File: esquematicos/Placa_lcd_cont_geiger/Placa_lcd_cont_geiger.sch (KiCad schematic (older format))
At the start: 17 parts, among them J1 Conn_02x04_Counter_Clockwise, J2 Conn_01x14_Female, J3 Conn_01x04_Female, P1 Power, P2 Analog, P3 Digital, P4 Digital, Q1 BC548, Q2 BC548

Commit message: Agregado del PCB del teclado(2)
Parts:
- J3: footprint Connector_JST:JST_EH_B04B-EH-A_1x04_P2.50mm_Vertical -> Connector_JST:JST_XH_B04B-XH-A_1x04_P2.50mm_Vertical
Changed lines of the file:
@@
 F 0 "J3" V 3940 3612 50  0000 R CNN
 F 1 "Conn_01x04_Female" V 3849 3612 50  0000 R CNN
-F 2 "Connector_JST:JST_EH_B04B-EH-A_1x04_P2.50mm_Vertical" H 4000 3900 50  0001 C CNN
+F 2 "Connector_JST:JST_XH_B04B-XH-A_1x04_P2.50mm_Vertical" H 4000 3900 50  0001 C CNN
 F 3 "~" H 4000 3900 50  0001 C CNN
 	1    4000 3900

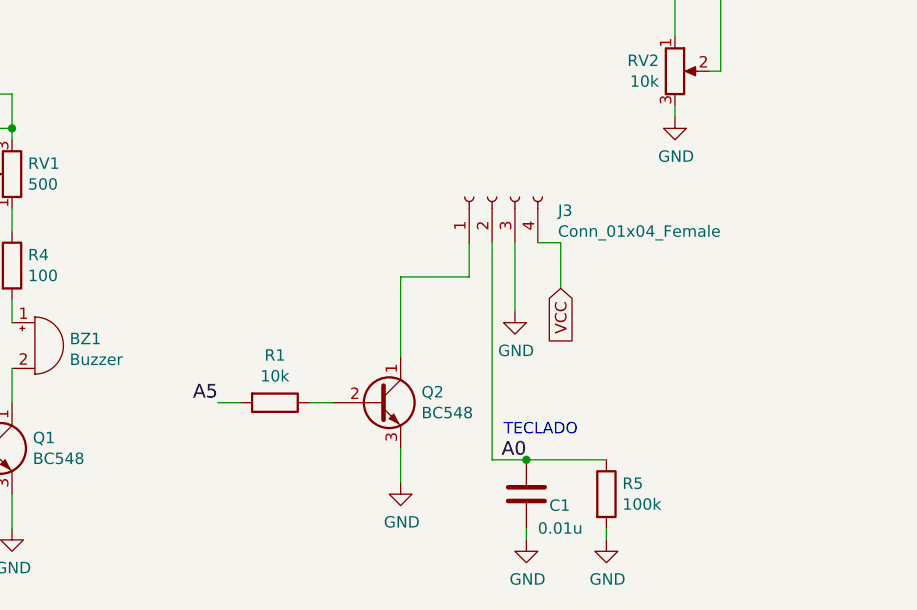
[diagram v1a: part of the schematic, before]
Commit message: Agregado de LED verde a la placa del teclado e incremento de las dimensiones de esta última incluyendo una mayor separación entre los botones
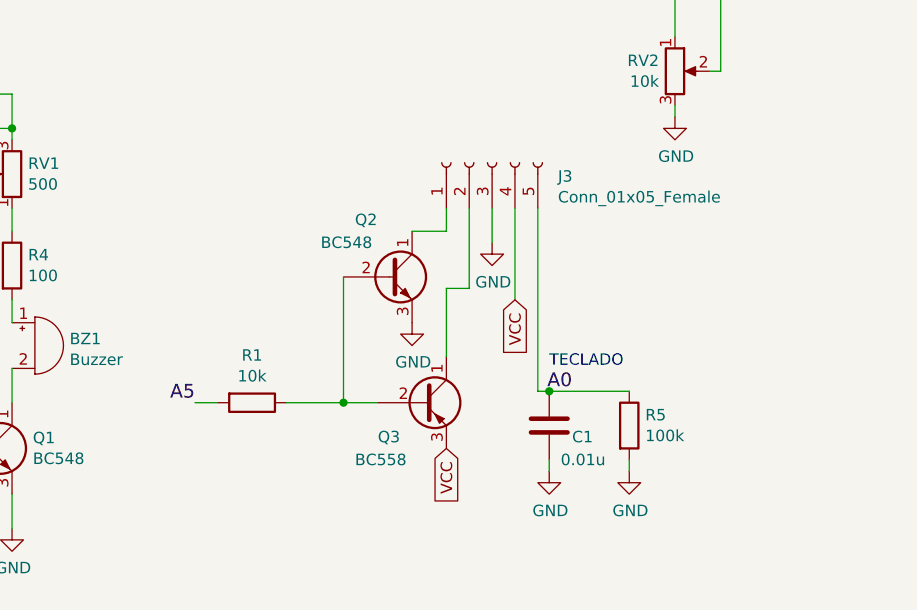
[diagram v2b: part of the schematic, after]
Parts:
- removed J3: Conn_01x04_Female, Connector_JST:JST_XH_B04B-XH-A_1x04_P2.50mm_Vertical, symbol Connector:Conn_01x04_Female
- added J3: Conn_01x05_Female, Connector_JST:JST_XH_B05B-XH-A_1x05_P2.50mm_Vertical, symbol Connector:Conn_01x05_Female
- added Q3: BC558, Package_TO_SOT_THT:TO-92_Inline, symbol Transistor_BJT:BC558
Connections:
- net +5V: now also J3.4 (Pin_4), Q3.3 (E)
- net A0: now also J3.5 (Pin_5)
- net GND: now also J3.3 (Pin_3)
- net at Q2.2 (B), R1.1: now also Q3.2 (B)
- net at Q2.1 (C): now also J3.1 (Pin_1)
- new net: J3.2 (Pin_2), Q3.1 (C)
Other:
- moved on the sheet: C1, Q2, R1, R5
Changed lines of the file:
@@
 	8250 1850 8100 1850
-$Comp
-L power:GND #PWR05
-U 1 1 5D57300A
-P 3600 5150
-F 0 "#PWR05" H 3600 4900 50  0001 C CNN
-F 1 "GND" H 3605 4977 50  0000 C CNN
-F 2 "" H 3600 5150 50  0001 C CNN
-F 3 "" H 3600 5150 50  0001 C CNN
-	1    3600 5150
-	1    0    0    -1
-$EndComp
-Wire Wire Line
-	3600 5150 3600 5000
 $Comp
 L Device:R R1
 U 1 1 5D574156
-P 3050 4800
-F 0 "R1" V 2843 4800 50  0000 C CNN
-F 1 "10k" V 2934 4800 50  0000 C CNN
-F 2 "Resistor_THT:R_Axial_DIN0207_L6.3mm_D2.5mm_P10.16mm_Horizontal" V 2980 4800 50  0001 C CNN
-F 3 "~" H 3050 4800 50  0001 C CNN
-	1    3050 4800
+P 2950 4800
+F 0 "R1" V 2743 4800 50  0000 C CNN
+F 1 "10k" V 2834 4800 50  0000 C CNN
+F 2 "Resistor_THT:R_Axial_DIN0207_L6.3mm_D2.5mm_P10.16mm_Horizontal" V 2880 4800 50  0001 C CNN
+F 3 "~" H 2950 4800 50  0001 C CNN
+	1    2950 4800
 	0    1    1    0
 $EndComp
-Wire Wire Line
-	3300 4800 3200 4800
-Wire Wire Line
-	2900 4800 2800 4800
 Text GLabel 1800 3450 0    50   Input ~ 0
 VCC
@@
 Wire Wire Line
 	2300 2000 2300 2050
-Text GLabel 4300 4300 3    50   Input ~ 0
+Text GLabel 4100 4350 3    50   Input ~ 0
 VCC
-Wire Wire Line
-	4300 4300 4300 4100
-Wire Wire Line
-	4300 4100 4200 4100
 $Comp
 L power:GND #PWR013
 U 1 1 5D5B0045
-P 4100 4400
-F 0 "#PWR013" H 4100 4150 50  0001 C CNN
-F 1 "GND" H 4105 4227 50  0000 C CNN
-F 2 "" H 4100 4400 50  0001 C CNN
-F 3 "" H 4100 4400 50  0001 C CNN
-	1    4100 4400
-	1    0    0    -1
-$EndComp
-Wire Wire Line
-	4100 4400 4100 4100
+P 4000 4100
+F 0 "#PWR013" H 4000 3850 50  0001 C CNN
+F 1 "GND" H 4005 3927 50  0000 C CNN
+F 2 "" H 4000 4100 50  0001 C CNN
+F 3 "" H 4000 4100 50  0001 C CNN
+	1    4000 4100
+	1    0    0    -1
+$EndComp
 $Comp
 L Device:R R5
 U 1 1 5D5B29A8
-P 4500 5200
-F 0 "R5" H 4570 5246 50  0000 L CNN
-F 1 "100k" H 4570 5155 50  0000 L CNN
-F 2 "Resistor_THT:R_Axial_DIN0207_L6.3mm_D2.5mm_P10.16mm_Horizontal" V 4430 5200 50  0001 C CNN
-F 3 "~" H 4500 5200 50  0001 C CNN
-	1    4500 5200
+P 4600 4900
+F 0 "R5" H 4670 4946 50  0000 L CNN
+F 1 "100k" H 4670 4855 50  0000 L CNN
+F 2 "Resistor_THT:R_Axial_DIN0207_L6.3mm_D2.5mm_P10.16mm_Horizontal" V 4530 4900 50  0001 C CNN
+F 3 "~" H 4600 4900 50  0001 C CNN
+	1    4600 4900
 	1    0    0    -1
 $EndComp
@@
 L Device:C C1
 U 1 1 5D5B30AC
-P 4150 5200
-F 0 "C1" H 4250 5150 50  0000 L CNN
-F 1 "0.01u" H 4200 5050 50  0000 L CNN
-F 2 "Capacitor_THT:C_Axial_L5.1mm_D3.1mm_P7.50mm_Horizontal" H 4188 5050 50  0001 C CNN
-F 3 "~" H 4150 5200 50  0001 C CNN
-	1    4150 5200
+P 4250 4900
+F 0 "C1" H 4350 4850 50  0000 L CNN
+F 1 "0.01u" H 4300 4750 50  0000 L CNN
+F 2 "Capacitor_THT:C_Axial_L5.1mm_D3.1mm_P7.50mm_Horizontal" H 4288 4750 50  0001 C CNN
+F 3 "~" H 4250 4900 50  0001 C CNN
+	1    4250 4900
 	1    0    0    -1
 $EndComp
@@
 L power:GND #PWR012
 U 1 1 5D5BA3C4
-P 4500 5400
-F 0 "#PWR012" H 4500 5150 50  0001 C CNN
-F 1 "GND" H 4505 5227 50  0000 C CNN
-F 2 "" H 4500 5400 50  0001 C CNN
-F 3 "" H 4500 5400 50  0001 C CNN
-	1    4500 5400
-	1    0    0    -1
-$EndComp
-Wire Wire Line
-	4500 5400 4500 5350
+P 4600 5100
+F 0 "#PWR012" H 4600 4850 50  0001 C CNN
+F 1 "GND" H 4605 4927 50  0000 C CNN
+F 2 "" H 4600 5100 50  0001 C CNN
+F 3 "" H 4600 5100 50  0001 C CNN
+	1    4600 5100
+	1    0    0    -1
+$EndComp
+Wire Wire Line
+	4600 5100 4600 5050
 $Comp
 L power:GND #PWR011
 U 1 1 5D5BCCB6
-P 4150 5400
-F 0 "#PWR011" H 4150 5150 50  0001 C CNN
-F 1 "GND" H 4155 5227 50  0000 C CNN
-F 2 "" H 4150 5400 50  0001 C CNN
-F 3 "" H 4150 5400 50  0001 C CNN
-	1    4150 5400
-	1    0    0    -1
-$EndComp
-Wire Wire Line
-	4150 5400 4150 5350
-Text Label 4150 5050 2    60   ~ 0
-A0
-Text Notes 4050 4950 0    50   ~ 0
+P 4250 5100
+F 0 "#PWR011" H 4250 4850 50  0001 C CNN
+F 1 "GND" H 4255 4927 50  0000 C CNN
+F 2 "" H 4250 5100 50  0001 C CNN
+F 3 "" H 4250 5100 50  0001 C CNN
+	1    4250 5100
+	1    0    0    -1
+$EndComp
+Wire Wire Line
+	4250 5100 4250 5050
+Text Notes 4250 4650 0    50   ~ 0
 TECLADO
 Wire Wire Line
-	4150 5050 4500 5050
-$Comp
-L Connector:Conn_01x04_Female J3
-U 1 1 5D58CA04
-P 4000 3900
-F 0 "J3" V 3940 3612 50  0000 R CNN
-F 1 "Conn_01x04_Female" V 3849 3612 50  0000 R CNN
-F 2 "Connector_JST:JST_XH_B04B-XH-A_1x04_P2.50mm_Vertical" H 4000 3900 50  0001 C CNN
-F 3 "~" H 4000 3900 50  0001 C CNN
-	1    4000 3900
-	0    -1   -1   0
-$EndComp
-Wire Wire Line
-	4150 5050 4000 5050
-Wire Wire Line
-	4000 4100 4000 5050
-Connection ~ 4150 5050
-Wire Wire Line
-	3600 4600 3600 4250
-Wire Wire Line
-	3600 4250 3900 4250
-Wire Wire Line
-	3900 4250 3900 4100
+	4250 4750 4600 4750
 $Comp
 L Transistor_BJT:BC548 Q1
@@
 L Transistor_BJT:BC548 Q2
 U 1 1 5D5A183A
-P 3500 4800
-F 0 "Q2" H 3691 4846 50  0000 L CNN
-F 1 "BC548" H 3691 4755 50  0000 L CNN
-F 2 "Package_TO_SOT_THT:TO-92_Inline" H 3700 4725 50  0001 L CIN
-F 3 "http://www.fairchildsemi.com/ds/BC/BC547.pdf" H 3500 4800 50  0001 L CNN
-	1    3500 4800
+P 3550 4250
+F 0 "Q2" H 3400 4500 50  0000 L CNN
+F 1 "BC548" H 3250 4400 50  0000 L CNN
+F 2 "Package_TO_SOT_THT:TO-92_Inline" H 3750 4175 50  0001 L CIN
+F 3 "http://www.fairchildsemi.com/ds/BC/BC547.pdf" H 3550 4250 50  0001 L CNN
+	1    3550 4250
 	1    0    0    -1
 $EndComp
@@
 Text Label 1100 5000 2    60   ~ 0
 A4
-Text Label 2800 4800 2    60   ~ 0
+Text Label 2700 4800 2    60   ~ 0
 A5
 NoConn ~ 10550 1800
@@
 Wire Wire Line
 	4900 1850 4900 2650
+$Comp
+L Transistor_BJT:BC558 Q3
+U 1 1 5D6006A5
+P 3700 4800
+F 0 "Q3" H 3500 4650 50  0000 L CNN
+F 1 "BC558" H 3400 4550 50  0000 L CNN
+F 2 "Package_TO_SOT_THT:TO-92_Inline" H 3900 4725 50  0001 L CIN
+F 3 "http://www.fairchildsemi.com/ds/BC/BC557.pdf" H 3700 4800 50  0001 L CNN
+	1    3700 4800
+	1    0    0    -1
+$EndComp
+$Comp
+L Connector:Conn_01x05_Female J3
+U 1 1 5D602E50
+P 4000 3750
+F 0 "J3" V 3940 3462 50  0000 R CNN
+F 1 "Conn_01x05_Female" V 3849 3462 50  0000 R CNN
+F 2 "Connector_JST:JST_XH_B05B-XH-A_1x05_P2.50mm_Vertical" H 4000 3750 50  0001 C CNN
+F 3 "~" H 4000 3750 50  0001 C CNN
+	1    4000 3750
+	0    -1   -1   0
+$EndComp
+Text GLabel 3800 5000 3    50   Input ~ 0
+VCC
+Wire Wire Line
+	2700 4800 2800 4800
+Wire Wire Line
+	3100 4800 3350 4800
+$Comp
+L power:GND #PWR?
+U 1 1 5D63E8E4
+P 3650 4450
+F 0 "#PWR?" H 3650 4200 50  0001 C CNN
+F 1 "GND" H 3655 4277 50  0000 C CNN
+F 2 "" H 3650 4450 50  0001 C CNN
+F 3 "" H 3650 4450 50  0001 C CNN
+	1    3650 4450
+	1    0    0    -1
+$EndComp
+Wire Wire Line
+	3650 4050 3800 4050
+Wire Wire Line
+	3800 4050 3800 3950
+Wire Wire Line
+	3800 4300 3900 4300
+Wire Wire Line
+	3900 4300 3900 3950
+Wire Wire Line
+	3800 4300 3800 4600
+Wire Wire Line
+	3350 4250 3350 4800
+Connection ~ 3350 4800
+Wire Wire Line
+	3350 4800 3500 4800
+Wire Wire Line
+	4000 3950 4000 4100
+Wire Wire Line
+	4100 3950 4100 4350
+Text Label 4350 4750 2    60   ~ 0
+A0
+Wire Wire Line
+	4200 3950 4200 4750
+Wire Wire Line
+	4200 4750 4250 4750
+Connection ~ 4250 4750
 $EndSCHEMATC

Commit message: Agrega PCB del teclado
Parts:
- J3: footprint Connector_JST:JST_XH_B05B-XH-A_1x05_P2.50mm_Vertical -> Connectors_Molex:Molex_KK-6410-05_05x2.54mm_Straight
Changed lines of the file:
@@
 F 0 "J3" V 3940 3462 50  0000 R CNN
 F 1 "Conn_01x05_Female" V 3849 3462 50  0000 R CNN
-F 2 "Connector_JST:JST_XH_B05B-XH-A_1x05_P2.50mm_Vertical" H 4000 3750 50  0001 C CNN
+F 2 "Connectors_Molex:Molex_KK-6410-05_05x2.54mm_Straight" H 4000 3750 50  0001 C CNN
 F 3 "~" H 4000 3750 50  0001 C CNN
 	1    4000 3750
@@
 	3100 4800 3350 4800
 $Comp
-L power:GND #PWR?
+L power:GND #PWR0101
 U 1 1 5D63E8E4
 P 3650 4450
-F 0 "#PWR?" H 3650 4200 50  0001 C CNN
+F 0 "#PWR0101" H 3650 4200 50  0001 C CNN
 F 1 "GND" H 3655 4277 50  0000 C CNN
 F 2 "" H 3650 4450 50  0001 C CNN
